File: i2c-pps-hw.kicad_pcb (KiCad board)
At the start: 2 copper layers, 85 x 56 mm, 6 parts

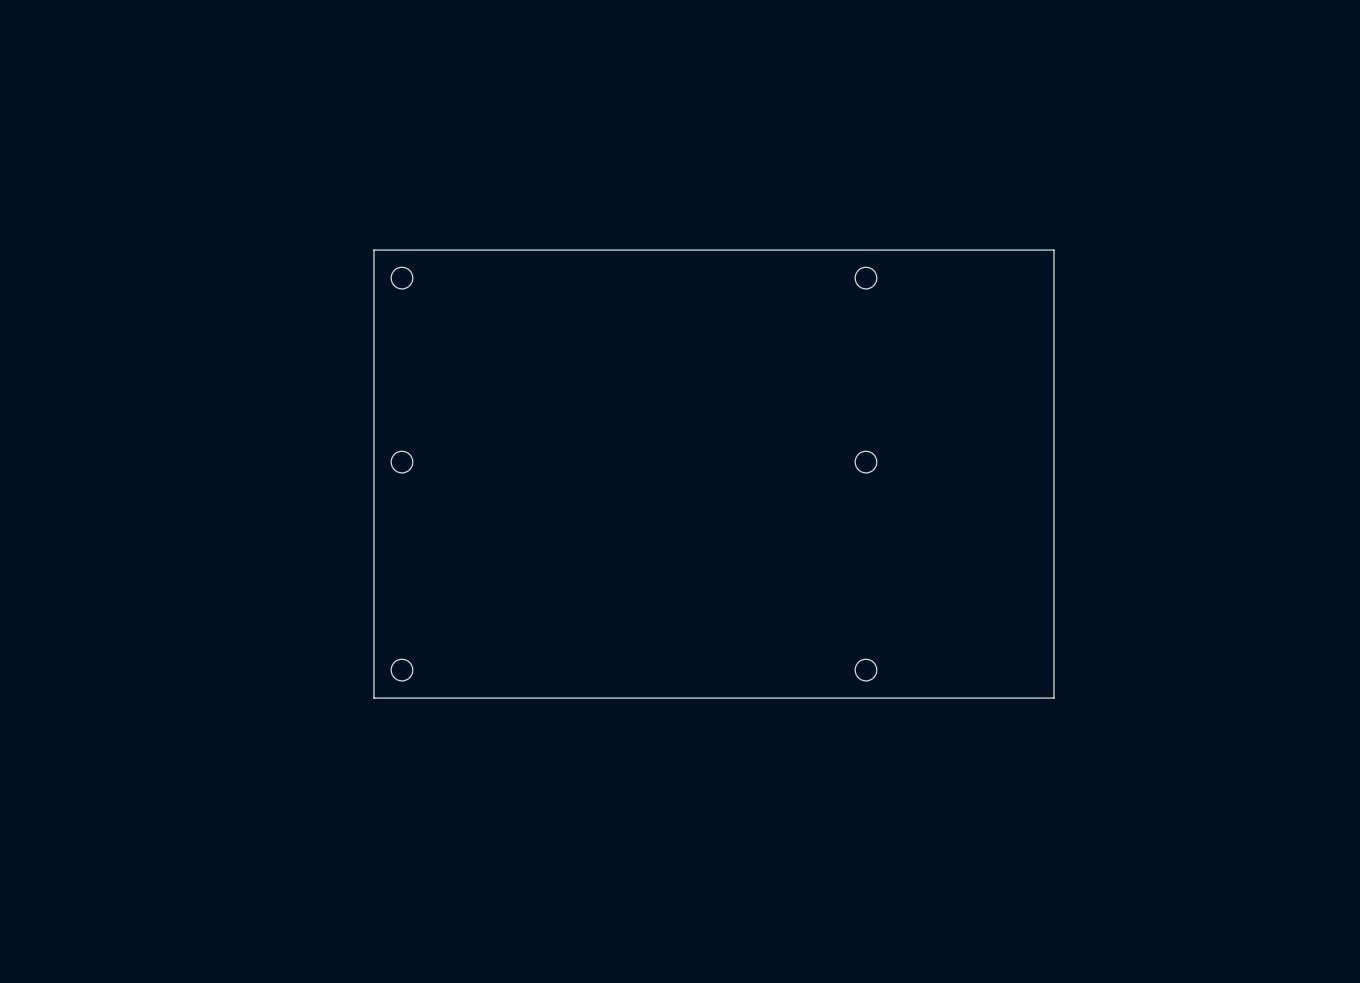
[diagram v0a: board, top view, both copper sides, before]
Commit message: Setup the board and move components from schematics
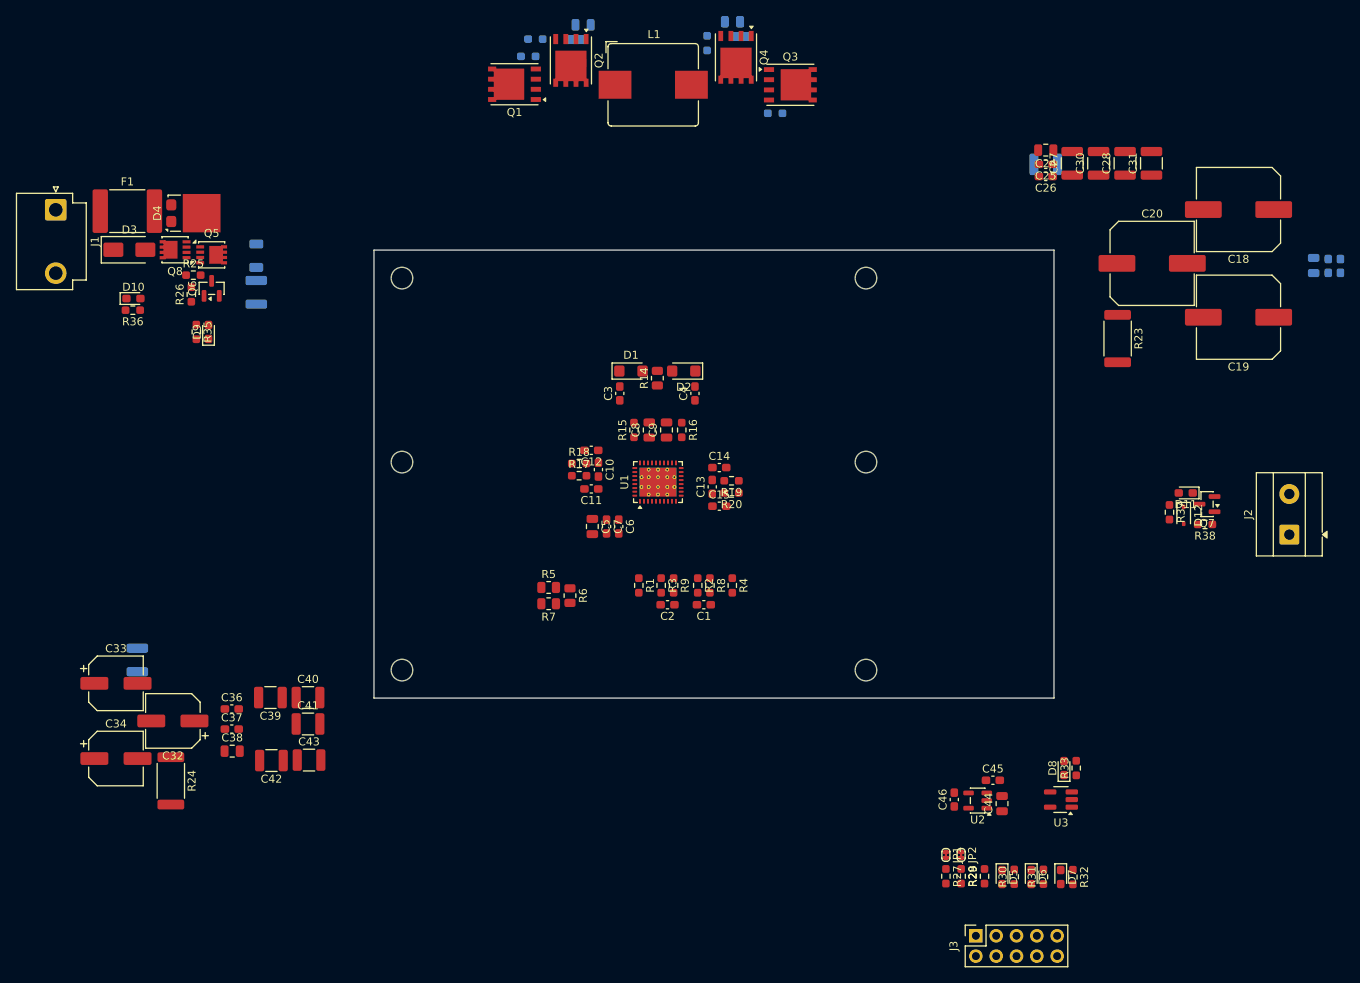
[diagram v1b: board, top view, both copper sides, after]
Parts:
- added C1: 0.1uF, Capacitor_SMD:C_0603_1608Metric_Pad1.08x0.95mm_HandSolder, F.Cu at (143.7, 124.3)
- added C10: 0.47uF, Capacitor_SMD:C_0603_1608Metric_Pad1.08x0.95mm_HandSolder, F.Cu at (130.6, 107.4)
- added C11: 0.1uF, Capacitor_SMD:C_0603_1608Metric_Pad1.08x0.95mm_HandSolder, F.Cu at (129.7, 109.9)
- added C12: 0.1uF, Capacitor_SMD:C_0603_1608Metric_Pad1.08x0.95mm_HandSolder, F.Cu at (129.7, 105.0)
- added C13: 0.47uF, Capacitor_SMD:C_0603_1608Metric_Pad1.08x0.95mm_HandSolder, F.Cu at (144.8, 109.6)
- added C14: 0.1uF, Capacitor_SMD:C_0603_1608Metric_Pad1.08x0.95mm_HandSolder, F.Cu at (145.7, 107.2)
- added C15: 0.1uF, Capacitor_SMD:C_0603_1608Metric_Pad1.08x0.95mm_HandSolder, F.Cu at (145.7, 112.0)
- added C16: ~, Capacitor_SMD:C_0805_2012Metric, B.Cu at (128.6, 51.8)
- added C17: ~, Capacitor_SMD:C_0805_2012Metric, B.Cu at (147.3, 51.5)
- added C18: 56uF, Capacitor_SMD:C_Elec_10x10.2, F.Cu at (210.6, 74.9)
- added C19: 56uF, Capacitor_SMD:C_Elec_10x10.2, F.Cu at (210.6, 88.4)
- added C2: 0.1uF, Capacitor_SMD:C_0603_1608Metric_Pad1.08x0.95mm_HandSolder, F.Cu at (139.2, 124.3)
- added C20: 56uF, Capacitor_SMD:C_Elec_10x10.2, F.Cu at (199.8, 81.7)
- added C21: 1nF, Capacitor_SMD:C_0603_1608Metric_Pad1.08x0.95mm_HandSolder, B.Cu at (223.3, 82.0)
- added C22: 0.1uF, Capacitor_SMD:C_0603_1608Metric_Pad1.08x0.95mm_HandSolder, B.Cu at (221.8, 82.0)
- added C23: 1uF, Capacitor_SMD:C_0805_2012Metric, B.Cu at (220.0, 81.9)
- added C24: 1uF, Capacitor_SMD:C_0805_2012Metric, F.Cu at (186.5, 67.5)
- added C25: 0.1uF, Capacitor_SMD:C_0603_1608Metric_Pad1.08x0.95mm_HandSolder, F.Cu at (186.5, 69.3)
- added C26: 100pF, Capacitor_SMD:C_0603_1608Metric_Pad1.08x0.95mm_HandSolder, F.Cu at (186.5, 70.8)
- added C27: 10uF, Capacitor_SMD:C_1210_3225Metric, F.Cu at (189.8, 69.2)
- added C28: 10uF, Capacitor_SMD:C_1210_3225Metric, F.Cu at (196.4, 69.2)
- added C29: 10uF, Capacitor_SMD:C_1210_3225Metric, B.Cu at (186.5, 69.3)
- added C3: 0.1uF, Capacitor_SMD:C_0603_1608Metric_Pad1.08x0.95mm_HandSolder, F.Cu at (133.2, 97.9)
- added C30: 4.7uF, Capacitor_SMD:C_1210_3225Metric, F.Cu at (193.1, 69.2)
- added C31: 4.7uF, Capacitor_SMD:C_1210_3225Metric, F.Cu at (199.7, 69.2)
- added C32: 47uF, Capacitor_SMD:CP_Elec_6.3x5.7, F.Cu at (77.4, 138.9)
- added C33: 47uF, Capacitor_SMD:CP_Elec_6.3x5.7, F.Cu at (70.2, 134.2)
- added C34: 47uF, Capacitor_SMD:CP_Elec_6.3x5.7, F.Cu at (70.2, 143.6)
- added C35: 4.7uF, Capacitor_SMD:C_1210_3225Metric, B.Cu at (72.9, 131.2)
- added C36: 100pF, Capacitor_SMD:C_0603_1608Metric_Pad1.08x0.95mm_HandSolder, F.Cu at (84.7, 137.4)
- added C37: 0.1uF, Capacitor_SMD:C_0603_1608Metric_Pad1.08x0.95mm_HandSolder, F.Cu at (84.7, 139.9)
- added C38: 1uF, Capacitor_SMD:C_0805_2012Metric, F.Cu at (84.8, 142.6)
- added C39: 10uF, Capacitor_SMD:C_1210_3225Metric, F.Cu at (89.6, 135.9)
- added C4: 0.1uF, Capacitor_SMD:C_0603_1608Metric_Pad1.08x0.95mm_HandSolder, F.Cu at (142.6, 97.9)
- added C40: 10uF, Capacitor_SMD:C_1210_3225Metric, F.Cu at (94.3, 135.9)
- added C41: 10uF, Capacitor_SMD:C_1210_3225Metric, F.Cu at (94.3, 139.2)
- added C42: 4.7uF, Capacitor_SMD:C_1210_3225Metric, F.Cu at (89.7, 143.8)
- added C43: 4.7uF, Capacitor_SMD:C_1210_3225Metric, F.Cu at (94.4, 143.8)
- added C44: 1uF, Capacitor_SMD:C_0805_2012Metric, F.Cu at (181.0, 149.2)
- added C45: 100pF, Capacitor_SMD:C_0603_1608Metric_Pad1.08x0.95mm_HandSolder, F.Cu at (179.9, 146.3)
- added C46: 2.2uF, Capacitor_SMD:C_0603_1608Metric_Pad1.08x0.95mm_HandSolder, F.Cu at (175.0, 148.7)
- added C47: 2.2uF, Capacitor_SMD:C_1210_3225Metric, B.Cu at (87.8, 85.3)
- added C5: 1uF, Capacitor_SMD:C_0805_2012Metric, F.Cu at (129.8, 114.6)
- added C6: 0.1uF, Capacitor_SMD:C_0603_1608Metric_Pad1.08x0.95mm_HandSolder, F.Cu at (133.1, 114.6)
- added C7: 0.1uF, Capacitor_SMD:C_0603_1608Metric_Pad1.08x0.95mm_HandSolder, F.Cu at (131.6, 114.6)
- added C8: 4.7uF, Capacitor_SMD:C_0805_2012Metric, F.Cu at (136.9, 102.5)
- added C9: 4.7uF, Capacitor_SMD:C_0805_2012Metric, F.Cu at (139.1, 102.5)
- added D1: V1FM10-M3/H, Diode_SMD:D_SMF, F.Cu at (134.6, 95.1)
- added D10: Yellow, LED_SMD:LED_0603_1608Metric_Pad1.05x0.95mm_HandSolder, F.Cu at (72.4, 86.1)
- added D11: Blue, LED_SMD:LED_0603_1608Metric_Pad1.05x0.95mm_HandSolder, F.Cu at (204.0, 110.4)
- added D12: BZX384C2V4, Diode_SMD:D_SOD-323, F.Cu at (203.7, 113.2)
- added D2: V1FM10-M3/H, Diode_SMD:D_SMF, F.Cu at (141.2, 95.1)
- added D3: SMAJ6.5CA, Diode_SMD:D_SMA, F.Cu at (71.9, 80.0)
- added D4: 15A, 12V, Package_TO_SOT_SMD:TO-277A, F.Cu at (79.9, 75.4)
- added D5: Red, LED_SMD:LED_0603_1608Metric_Pad1.05x0.95mm_HandSolder, F.Cu at (181.0, 158.4)
- added D6: Green, LED_SMD:LED_0603_1608Metric_Pad1.05x0.95mm_HandSolder, F.Cu at (184.7, 158.4)
- added D7: Green, LED_SMD:LED_0603_1608Metric_Pad1.05x0.95mm_HandSolder, F.Cu at (188.3, 158.4)
- added D8: Green, LED_SMD:LED_0603_1608Metric_Pad1.05x0.95mm_HandSolder, F.Cu at (188.8, 144.7)
- added D9: Green, LED_SMD:LED_0603_1608Metric_Pad1.05x0.95mm_HandSolder, F.Cu at (81.8, 90.2)
- added F1: 5A, Fuse:Fuse_2920_7451Metric, F.Cu at (71.7, 75.1)
- added J1: +5V, i2c-pps-hw:TE_1-1123724-2, F.Cu at (62.7, 75.0)
- added J2: Vout, TerminalBlock_MetzConnect:TerminalBlock_MetzConnect_Type101_RT01602HBWC_1x02_P5.08mm_Horizontal, F.Cu at (216.9, 115.6)
- added J3: Digital I/O, Connector_PinSocket_2.54mm:PinSocket_2x05_P2.54mm_Vertical, F.Cu at (177.7, 165.7)
- added JP1: ~, i2c-pps-hw:SolderJumper-2_P0.65mm_Bridged_RoundedPad0.5x0.75mm, F.Cu at (174.0, 155.6)
- added JP2: ~, i2c-pps-hw:SolderJumper-2_P0.65mm_Bridged_RoundedPad0.5x0.75mm, F.Cu at (175.9, 155.6)
- added L1: 10uH, i2c-pps-hw:L_Bourns_SRP1038A_10.0x11.0mm, F.Cu at (137.4, 59.3)
- added Q1: SiR880BDP, Package_SO:PowerPAK_SO-8_Single, F.Cu at (120.1, 59.3)
- added Q2: SiR880BDP, Package_SO:PowerPAK_SO-8_Single, F.Cu at (127.1, 56.3)
- added Q3: SiR880BDP, Package_SO:PowerPAK_SO-8_Single, F.Cu at (154.5, 59.3)
- added Q4: SiR880BDP, Package_SO:PowerPAK_SO-8_Single, F.Cu at (147.8, 55.9)
- added Q5: SIS413DN, Package_SO:Vishay_PowerPAK_1212-8_Single, F.Cu at (82.2, 80.6)
- added Q6: MMBT3904, Package_TO_SOT_SMD:SOT-23, F.Cu at (82.2, 84.8)
- added Q7: MMBT3904, Package_TO_SOT_SMD:SOT-23, F.Cu at (206.6, 111.8)
- added Q8: SIS413DN, Package_SO:Vishay_PowerPAK_1212-8_Single, F.Cu at (77.6, 80.0)
- added R1: 133k, Resistor_SMD:R_0603_1608Metric_Pad0.98x0.95mm_HandSolder, F.Cu at (135.6, 121.9)
- added R10: 0, Resistor_SMD:R_0603_1608Metric_Pad0.98x0.95mm_HandSolder, B.Cu at (121.8, 55.8)
- added R11: 0, Resistor_SMD:R_0603_1608Metric_Pad0.98x0.95mm_HandSolder, B.Cu at (122.7, 53.6)
- added R12: 0, Resistor_SMD:R_0603_1608Metric_Pad0.98x0.95mm_HandSolder, B.Cu at (152.6, 62.9)
- added R13: 0, Resistor_SMD:R_0603_1608Metric_Pad0.98x0.95mm_HandSolder, B.Cu at (144.1, 54.1)
- added R14: 0, Resistor_SMD:R_0805_2012Metric, F.Cu at (137.9, 96.0)
- added R15: 0, Resistor_SMD:R_0603_1608Metric_Pad0.98x0.95mm_HandSolder, F.Cu at (135.0, 102.5)
- added R16: 0, Resistor_SMD:R_0603_1608Metric_Pad0.98x0.95mm_HandSolder, F.Cu at (141.0, 102.5)
- added R17: 10, Resistor_SMD:R_0603_1608Metric_Pad0.98x0.95mm_HandSolder, F.Cu at (128.1, 108.2)
- added R18: 10, Resistor_SMD:R_0603_1608Metric_Pad0.98x0.95mm_HandSolder, F.Cu at (128.1, 106.7)
- added R19: 10, Resistor_SMD:R_0603_1608Metric_Pad0.98x0.95mm_HandSolder, F.Cu at (147.2, 108.8)
- added R2: 3.92k, Resistor_SMD:R_0603_1608Metric_Pad0.98x0.95mm_HandSolder, F.Cu at (143.0, 121.9)
- added R20: 10, Resistor_SMD:R_0603_1608Metric_Pad0.98x0.95mm_HandSolder, F.Cu at (147.2, 110.4)
- added R21: ~, Resistor_SMD:R_1210_3225Metric, B.Cu at (127.8, 55.1)
- added R22: ~, Resistor_SMD:R_1210_3225Metric, B.Cu at (148.3, 54.8)
- added R23: 5m, Resistor_SMD:R_2512_6332Metric, F.Cu at (195.5, 91.1)
- added R24: 5m, Resistor_SMD:R_2512_6332Metric, F.Cu at (77.1, 146.4)
- added R25: 20k, Resistor_SMD:R_0603_1608Metric_Pad0.98x0.95mm_HandSolder, F.Cu at (79.9, 83.1)
- added R26: 10k, Resistor_SMD:R_0603_1608Metric_Pad0.98x0.95mm_HandSolder, F.Cu at (79.7, 85.5)
- added R27: 10k, Resistor_SMD:R_0603_1608Metric_Pad0.98x0.95mm_HandSolder, F.Cu at (174.0, 158.3)
- added R28: 10k, Resistor_SMD:R_0603_1608Metric_Pad0.98x0.95mm_HandSolder, F.Cu at (175.9, 158.3)
- added R29: 10k, Resistor_SMD:R_0603_1608Metric_Pad0.98x0.95mm_HandSolder, F.Cu at (178.8, 158.3)
- added R3: 10k, Resistor_SMD:R_0603_1608Metric_Pad0.98x0.95mm_HandSolder, F.Cu at (138.4, 121.9)
- added R30: 1k, Resistor_SMD:R_0603_1608Metric_Pad0.98x0.95mm_HandSolder, F.Cu at (182.5, 158.3)
- added R31: 1k, Resistor_SMD:R_0603_1608Metric_Pad0.98x0.95mm_HandSolder, F.Cu at (186.2, 158.3)
- added R32: 1k, Resistor_SMD:R_0603_1608Metric_Pad0.98x0.95mm_HandSolder, F.Cu at (189.9, 158.4)
- added R33: 1k, Resistor_SMD:R_0603_1608Metric_Pad0.98x0.95mm_HandSolder, F.Cu at (190.3, 144.7)
- added R34: 10, Resistor_SMD:R_1206_3216Metric, B.Cu at (87.8, 80.7)
- added R35: 1k, Resistor_SMD:R_0603_1608Metric_Pad0.98x0.95mm_HandSolder, F.Cu at (80.3, 90.2)
- added R36: 2.7k, Resistor_SMD:R_0603_1608Metric_Pad0.98x0.95mm_HandSolder, F.Cu at (72.4, 87.5)
- added R37: 20k, Resistor_SMD:R_0603_1608Metric_Pad0.98x0.95mm_HandSolder, F.Cu at (201.9, 112.8)
- added R38: 1k, Resistor_SMD:R_0603_1608Metric_Pad0.98x0.95mm_HandSolder, F.Cu at (206.4, 114.3)
- added R4: 3k, Resistor_SMD:R_0603_1608Metric_Pad0.98x0.95mm_HandSolder, F.Cu at (147.3, 121.9)
- added R5: 1M, Resistor_SMD:R_0805_2012Metric, F.Cu at (124.3, 122.2)
- added R6: 105k, Resistor_SMD:R_0805_2012Metric, F.Cu at (127.0, 123.2)
- added R7: 274k, Resistor_SMD:R_0805_2012Metric, F.Cu at (124.3, 124.2)
- added R8: 1.8k, Resistor_SMD:R_0603_1608Metric_Pad0.98x0.95mm_HandSolder, F.Cu at (144.5, 121.9)
- added R9: 1.8k, Resistor_SMD:R_0603_1608Metric_Pad0.98x0.95mm_HandSolder, F.Cu at (140.0, 121.9)
- added U1: BQ25758S, i2c-pps-hw:Texas_RRV0036A_VQFN-36-1EP_4.8x5.8mm_P0.5mm_EP3.6x4.6mm_ThermalVias, F.Cu at (138.0, 109.0)
- added U2: AP2210-3.3, Package_TO_SOT_SMD:SOT-23-5, F.Cu at (178.0, 148.8)
- added U3: 74AHC1G14, Package_TO_SOT_SMD:SOT-23-5_HandSoldering, F.Cu at (188.4, 148.7)
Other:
- copper layers 2 -> 4
